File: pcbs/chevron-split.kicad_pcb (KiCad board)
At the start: 2 copper layers, 163.8 x 118.2 mm, 135 parts

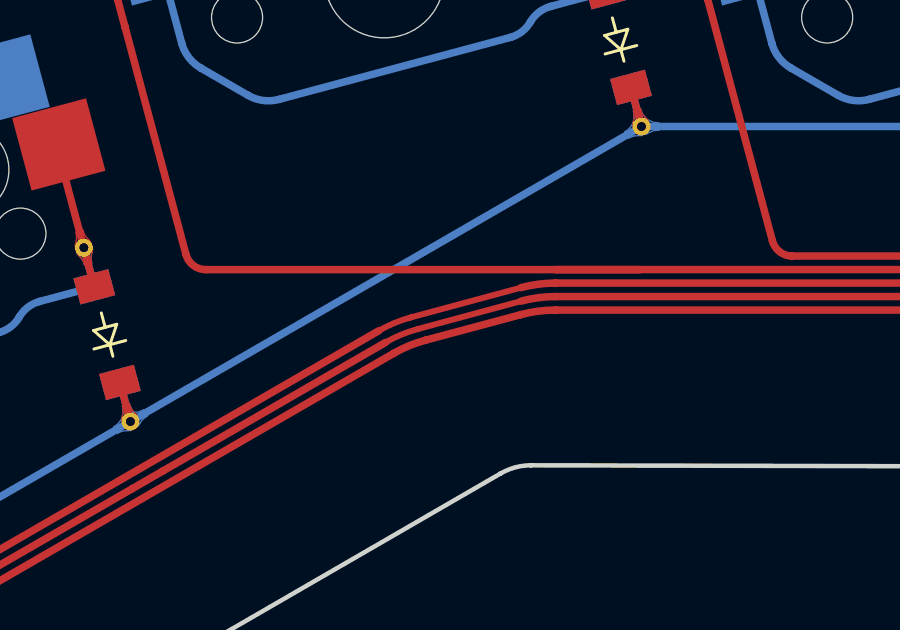
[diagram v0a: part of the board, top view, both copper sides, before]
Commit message: Snapshot of files for manufacturing prototype version 0.1 PCBs. Created left and right versions for faster prototype iteration.
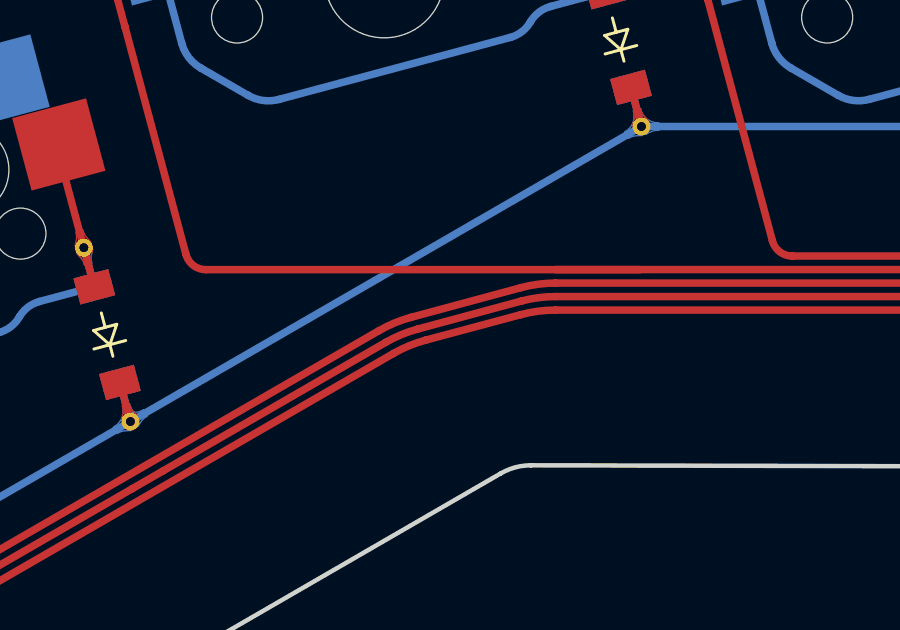
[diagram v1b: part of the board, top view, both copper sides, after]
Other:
- rule pad_to_mask_clearance: 0.05 -> 0
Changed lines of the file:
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@@
   )
   (setup
-    (pad_to_mask_clearance 0.05)
+    (stackup
+      (layer "F.SilkS" (type "Top Silk Screen"))
+      (layer "F.Paste" (type "Top Solder Paste"))
+      (layer "F.Mask" (type "Top Solder Mask") (thickness 0.01))
+      (layer "F.Cu" (type "copper") (thickness 0.035))
+      (layer "dielectric 1" (type "core") (thickness 1.51) (material "FR4") (epsilon_r 4.5) (loss_tangent 0.02))
+      (layer "B.Cu" (type "copper") (thickness 0.035))
+      (layer "B.Mask" (type "Bottom Solder Mask") (thickness 0.01))
+      (layer "B.Paste" (type "Bottom Solder Paste"))
+      (layer "B.SilkS" (type "Bottom Silk Screen"))
+      (copper_finish "None")
+      (dielectric_constraints no)
+    )
+    (pad_to_mask_clearance 0)
     (pcbplotparams
       (layerselection 0x00010fc_ffffffff)
       (disableapertmacros false)
-      (usegerberextensions false)
+      (usegerberextensions true)
       (usegerberattributes true)
       (usegerberadvancedattributes true)
@@
       (psa4output false)
       (plotreference true)
-      (plotvalue true)
+      (plotvalue false)
       (plotinvisibletext false)
       (sketchpadsonfab false)
-      (subtractmaskfromsilk false)
+      (subtractmaskfromsilk true)
       (outputformat 1)
       (mirror false)
-      (drillshape 1)
+      (drillshape 0)
       (scaleselection 1)
-      (outputdirectory "")
+      (outputdirectory "plots/")
     )
   )
@@
   (segment (start 94.733719 120.06056) (end 97.832848 121.849842) (width 0.25) (layer "F.Cu") (net 9))
   (segment (start 99.782373 119.53009) (end 103.026438 118.660847) (width 0.25) (layer "F.Cu") (net 9))
-  (segment (start 140.023392 117.454817) (end 143.468432 116.523879) (width 0.2) (layer "F.Cu") (net 9))
+  (segment (start 140.023392 117.454817) (end 143.468432 116.523879) (width 0.25) (layer "F.Cu") (net 9))
   (segment (start 193.479925 95.244378) (end 205.761649 82.962652) (width 0.25) (layer "F.Cu") (net 9))
   (segment (start 208.723715 101.880719) (end 210.531649 103.688653) (width 0.25) (layer "F.Cu") (net 9))
@@
   (arc (start 94.864808 101.177501) (mid 94.388751 101.412268) (end 94.038773 101.811342) (width 0.25) (layer "F.Cu") (net 9))
   (arc (start 85.029684 64.472318) (mid 84.553627 64.707084) (end 84.203649 65.106158) (width 0.25) (layer "F.Cu") (net 9))
-  (arc (start 140.023392 117.454817) (mid 139.474818 117.642008) (end 138.955099 117.898648) (width 0.2) (layer "F.Cu") (net 9))
+  (arc (start 140.023392 117.454817) (mid 139.474818 117.642008) (end 138.955099 117.898648) (width 0.25) (layer "F.Cu") (net 9))
   (arc (start 96.084681 125.102426) (mid 95.914062 125.605054) (end 95.948778 126.134714) (width 0.25) (layer "F.Cu") (net 9))
   (arc (start 208.721524 101.880719) (mid 208.42663 101.439378) (end 208.323078 100.91878) (width 0.25) (layer "F.Cu") (net 9))
@@
   (segment (start 116.817545 109.695872) (end 120.061617 108.826624) (width 0.25) (layer "F.Cu") (net 15))
   (segment (start 190.434291 113.14612) (end 192.233026 111.347383) (width 0.25) (layer "F.Cu") (net 15))
-  (segment (start 143.468418 116.073821) (end 139.798404 117.065162) (width 0.2) (layer "F.Cu") (net 15))
+  (segment (start 143.468418 116.073821) (end 139.798404 117.065162) (width 0.25) (layer "F.Cu") (net 15))
   (segment (start 138.730099 117.508935) (end 123.922161 126.058301) (width 0.25) (layer "F.Cu") (net 15))
   (arc (start 103.291203 78.587168) (mid 103.120584 79.089796) (end 103.1553 79.619456) (width 0.25) (layer "F.Cu") (net 15))
@@
   (arc (start 116.817545 109.695872) (mid 116.341488 109.930639) (end 115.99151 110.329713) (width 0.25) (layer "F.Cu") (net 15))
   (arc (start 115.014829 123.879832) (mid 115.259839 124.304201) (end 115.684208 124.549211) (width 0.25) (layer "F.Cu") (net 15))
-  (arc (start 139.798404 117.065162) (mid 139.249821 117.25231) (end 138.730099 117.508935) (width 0.2) (layer "F.Cu") (net 15))
+  (arc (start 139.798404 117.065162) (mid 139.249821 117.25231) (end 138.730099 117.508935) (width 0.25) (layer "F.Cu") (net 15))
   (arc (start 113.119854 115.268204) (mid 112.949235 115.770831) (end 112.983951 116.300491) (width 0.25) (layer "F.Cu") (net 15))
   (arc (start 101.331653 72.813525) (mid 101.566418 73.289582) (end 101.965492 73.639561) (width 0.25) (layer "F.Cu") (net 15))
